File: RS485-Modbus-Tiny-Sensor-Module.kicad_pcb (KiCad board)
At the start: 2 copper layers, 10 parts, among them SW1 FSM4JSMA, U2 ATtiny3216-S

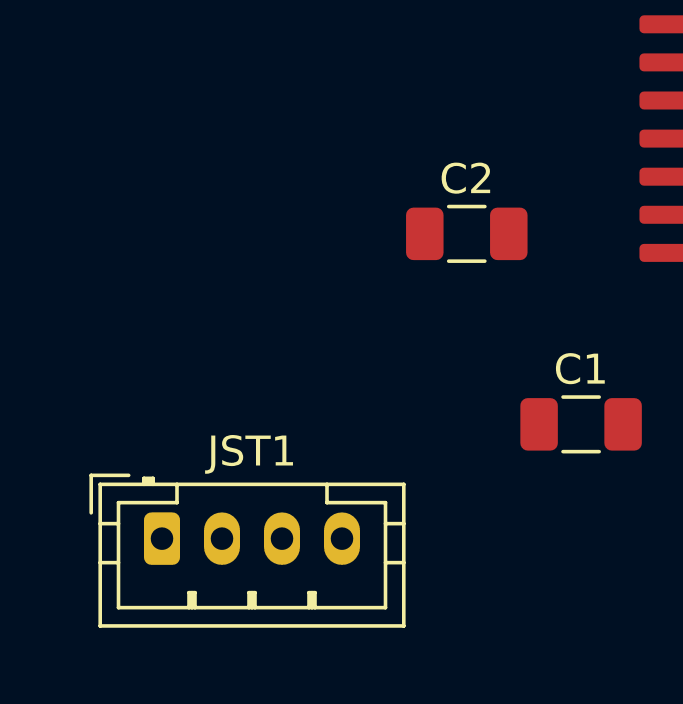
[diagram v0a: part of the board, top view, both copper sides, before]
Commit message: Add files via upload
Changed JST connection to smallest + fix connection to 3.3 V
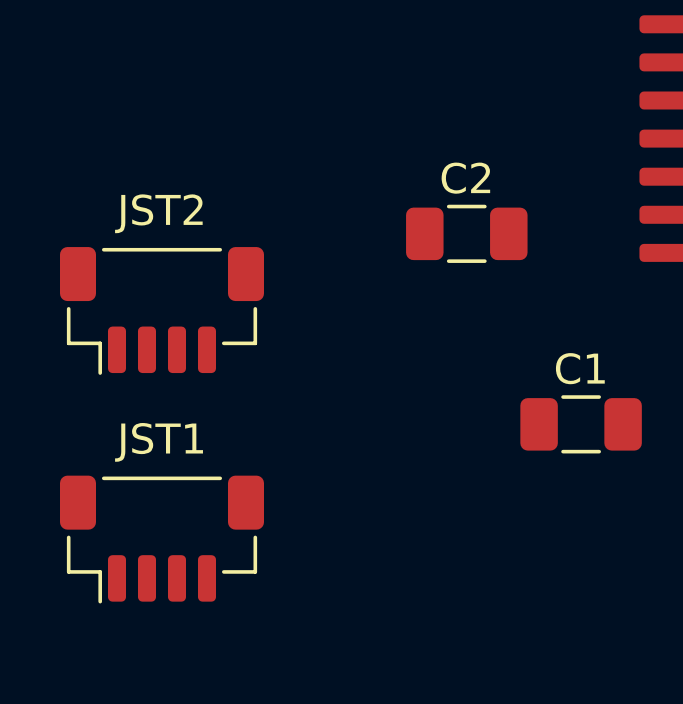
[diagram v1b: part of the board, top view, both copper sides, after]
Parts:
- added JST2: Conn_01x04, Connector_JST:JST_SH_BM04B-SRSS-TB_1x04-1MP_P1.00mm_Vertical, F.Cu at (99.1, 105.4)
- JST1: footprint Connector_JST:JST_PH_B4B-PH-K_1x04_P2.00mm_Vertical -> Connector_JST:JST_SH_BM04B-SRSS-TB_1x04-1MP_P1.00mm_Vertical
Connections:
- U2 pad 1: Net-(U2-Pad1) -> /3.3V

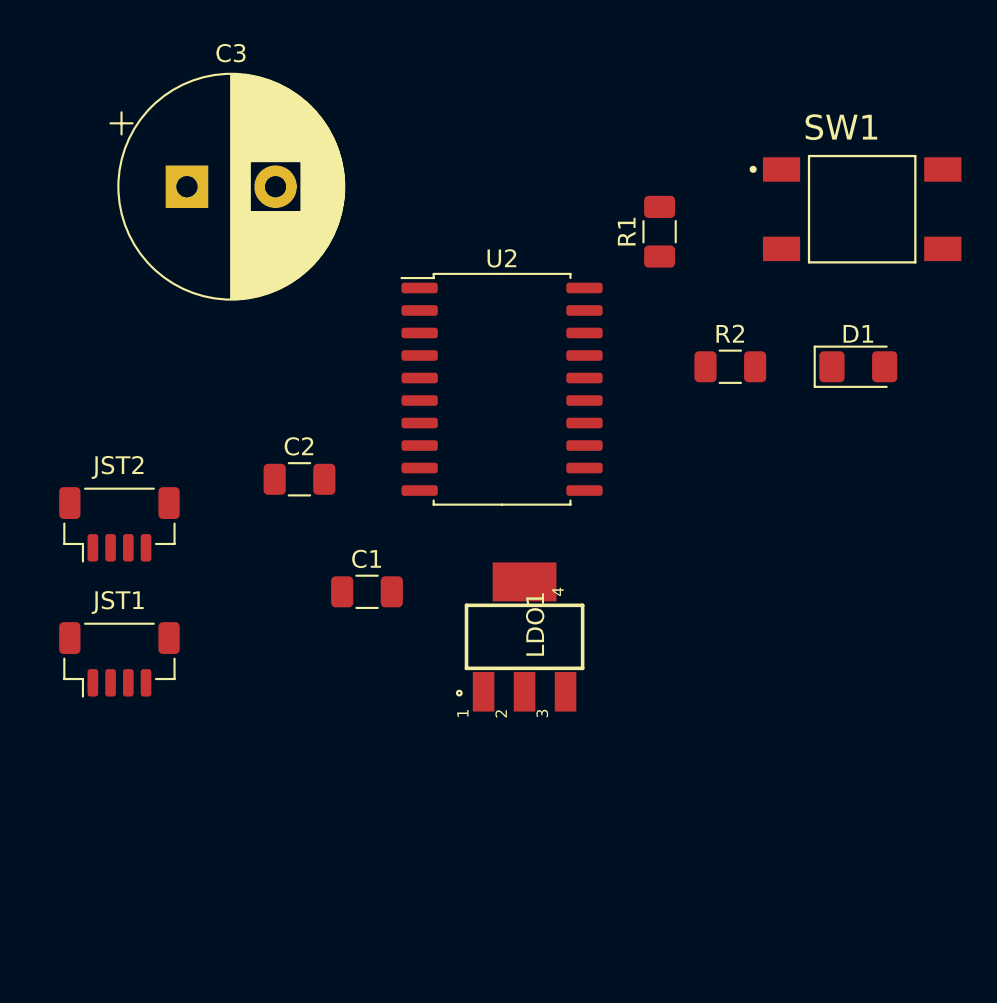
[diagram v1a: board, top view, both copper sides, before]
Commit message: Add files via upload
Added 24V LDO + cleaned layout + added autoreset
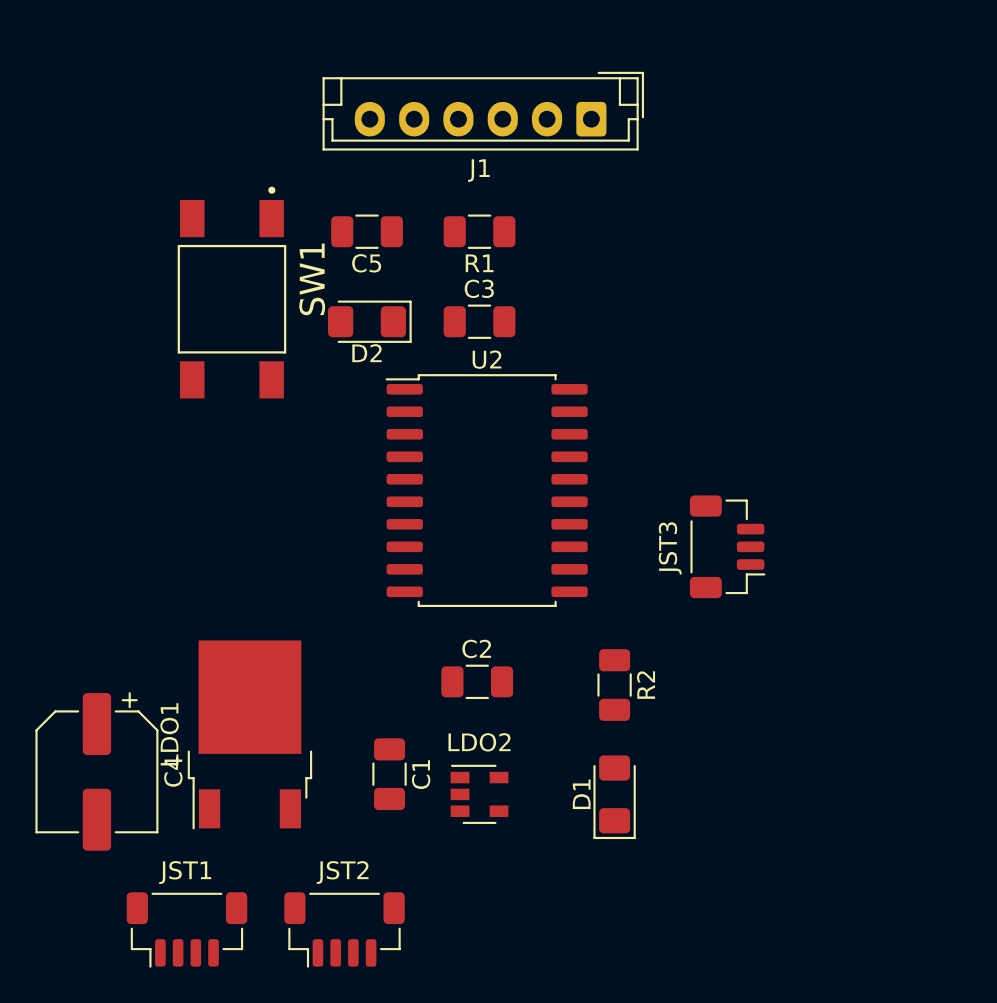
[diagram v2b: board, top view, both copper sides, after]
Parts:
- added C4: 100u, Capacitor_SMD:CP_Elec_6.3x7.7, F.Cu at (97.8, 119.4)
- added C5: 10u, Capacitor_SMD:C_1206_3216Metric, F.Cu at (113.0, 88.9)
- added D2: D, Diode_SMD:D_1206_3216Metric_Pad1.42x1.75mm_HandSolder, F.Cu at (113.0, 94.0)
- added J1: Conn_01x06, Connector_JST:JST_EH_B6B-EH-A_1x06_P2.50mm_Vertical, F.Cu at (125.7, 82.5)
- added JST3: Conn_01x03, Connector_JST:JST_SH_BM03B-SRSS-TB_1x03-1MP_P1.00mm_Vertical, F.Cu at (133.3, 106.7)
- added LDO2: MIC5504-3.3YM5, Package_TO_SOT_SMD:SOT-23-5, F.Cu at (119.4, 120.7)
- C1: value 10u -> 100u
- C3: value 2700u -> 100u; footprint Capacitor_THT:CP_Radial_D12.5mm_P5.00mm -> Capacitor_SMD:C_1206_3216Metric
- LDO1: value LM1117IMP-5.0-NOPB -> LD1086DT50TR; footprint LM1117IMP-5:SOT223 -> Package_TO_SOT_SMD:TO-252-2
- R2: value 200 -> 300
- moved SW1 35.9 mm to (105.4, 92.7), turned to 270 degrees
- moved D1 27.8 mm to (127.0, 120.7), turned to 90 degrees
- moved JST2 26.2 mm to (111.8, 128.3)
- moved R2 19.1 mm to (127.0, 114.5), turned to 270 degrees
- moved C3 18.2 mm to (119.4, 94.0)
- moved LDO1 16.4 mm to (106.4, 117.3)
- moved JST1 15.7 mm to (102.9, 128.3)
- moved C2 15.2 mm to (119.2, 114.3)
- moved C1 10.4 mm to (114.3, 119.5), turned to 270 degrees
- moved R1 10.2 mm to (119.4, 88.9), turned to 180 degrees
- moved U2 5.78 mm to (119.8, 103.5)
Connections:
- JST1 pad 2: /5V -> /24V
- JST2 pad 2: /5V -> /24V
- LDO1 pad 2: /3.3V -> /5V
- LDO1 pad 3: /5V -> /24V
- R1 pad 1: /3.3V -> /5V
- U2 pad 1: /3.3V -> /5V
- U2 pad 12: Net-(U2-Pad12) -> Net-(R2-Pad1)
- U2 pad 5: Net-(U2-Pad5) -> /PA7
- U2 pad 8: Net-(U2-Pad8) -> /RX
- U2 pad 9: Net-(U2-Pad9) -> /TX

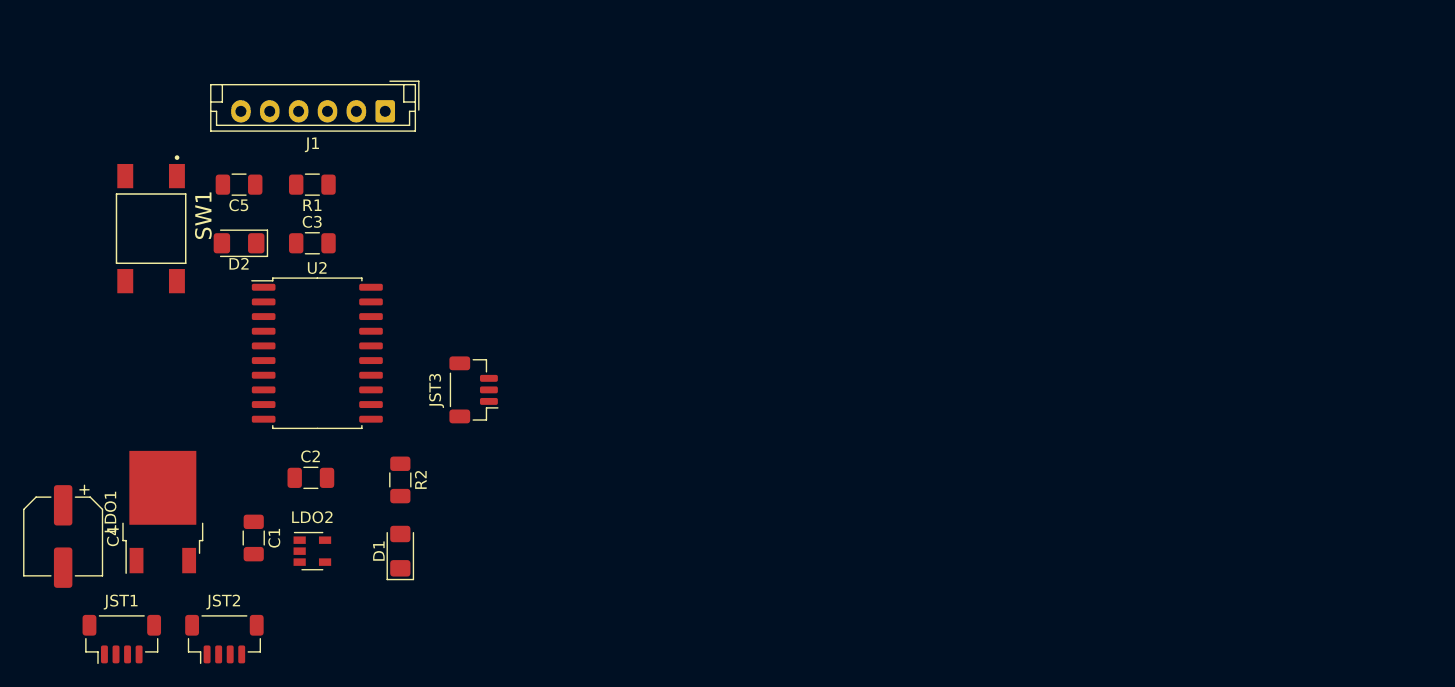
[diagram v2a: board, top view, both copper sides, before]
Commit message: Add files via upload
Finished layout prototype + added extra JST
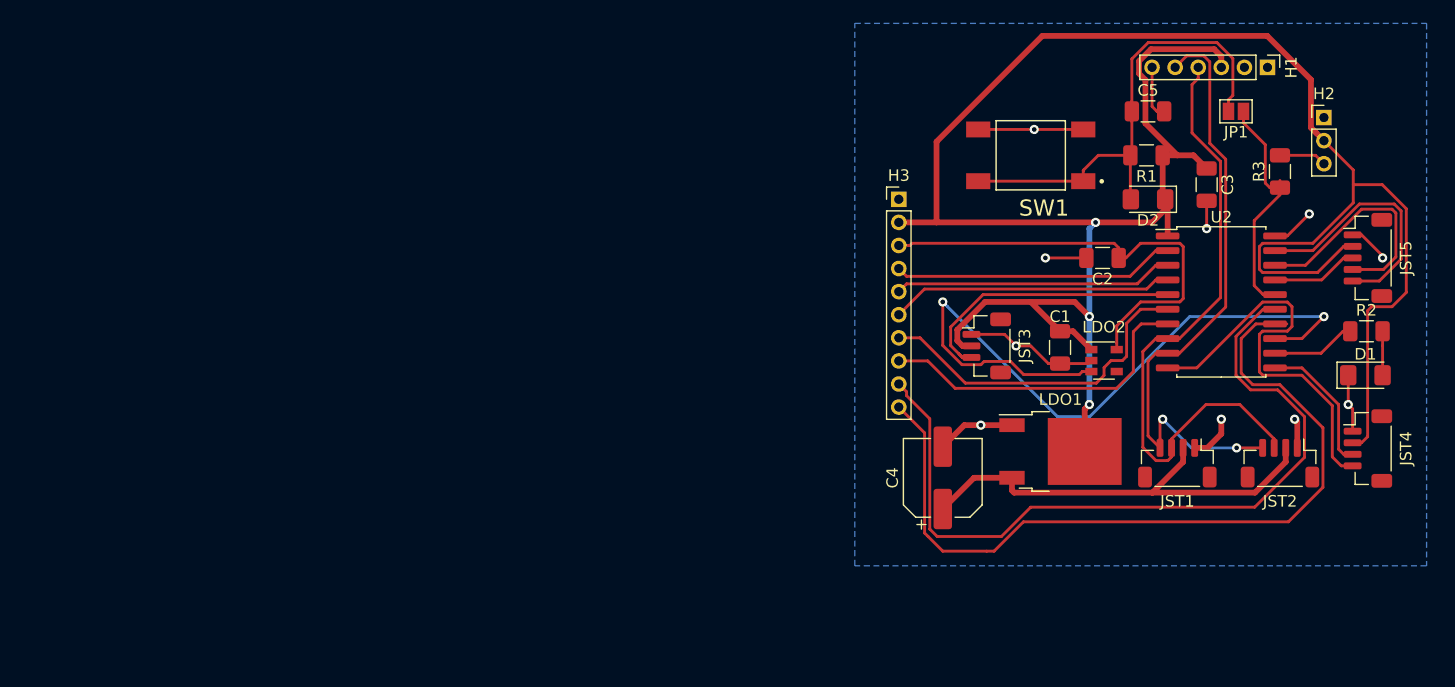
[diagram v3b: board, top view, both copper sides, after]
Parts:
- added H2: Conn_01x03, Connector_PinHeader_2.00mm:PinHeader_1x03_P2.00mm_Vertical, F.Cu at (207.0, 83.1)
- added H3: Conn_01x10, Connector_PinHeader_2.00mm:PinHeader_1x10_P2.00mm_Vertical, F.Cu at (170.2, 90.2)
- added JP1: Jumper, Jumper:SolderJumper-2_P1.3mm_Open_Pad1.0x1.5mm, F.Cu at (199.4, 82.5)
- added JST4: Conn_01x04, Connector_JST:JST_SH_BM04B-SRSS-TB_1x04-1MP_P1.00mm_Vertical, F.Cu at (210.8, 111.8)
- added JST5: Conn_01x05, Connector_JST:JST_SH_BM05B-SRSS-TB_1x05-1MP_P1.00mm_Vertical, F.Cu at (210.8, 95.2)
- added R3: 4.7k, Resistor_SMD:R_1206_3216Metric, F.Cu at (203.2, 87.8)
- C5: value 10u -> 1u
- H1: renamed from J1; footprint Connector_JST:JST_EH_B6B-EH-A_1x06_P2.50mm_Vertical -> Connector_PinHeader_2.00mm:PinHeader_1x06_P2.00mm_Vertical
- moved JST1 92.7 mm to (194.3, 113.0), turned to 180 degrees
- moved JST2 92.7 mm to (203.2, 113.0), turned to 180 degrees
- moved D1 85.0 mm to (210.6, 105.4), turned to 0 degrees
- moved R2 84.7 mm to (210.7, 101.6), turned to 0 degrees
- moved C5 79.0 mm to (191.8, 82.5), turned to 0 degrees
- moved D2 78.8 mm to (191.8, 90.2)
- moved U2 78.4 mm to (198.1, 99.1)
- moved LDO1 77.9 mm to (184.2, 112.0), turned to 0 degrees
- moved C3 77.6 mm to (196.8, 88.9), turned to 270 degrees
- moved H1 76.5 mm to (202.1, 78.7), turned to 270 degrees
- moved SW1 76.5 mm to (181.6, 86.4), turned to 180 degrees
- moved C4 76.4 mm to (174.0, 114.3), turned to 90 degrees
- moved R1 72.3 mm to (191.6, 86.4)
- moved C1 71.8 mm to (184.2, 103.0)
- moved C2 71.2 mm to (187.8, 95.2), turned to 180 degrees
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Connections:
- JST1 pad 3: Net-(JST1-Pad3) -> /RX
- JST1 pad 4: Net-(JST1-Pad4) -> /TX
- JST2 pad 3: Net-(JST2-Pad3) -> /RX
- JST2 pad 4: Net-(JST2-Pad4) -> /TX
- U2 pad 10: Net-(U2-Pad10) -> /SDA
- U2 pad 11: Net-(U2-Pad11) -> /SCL
- U2 pad 14: Net-(U2-Pad14) -> /PC2
- U2 pad 15: Net-(U2-Pad15) -> /PC3
- U2 pad 16: Net-(C5-Pad1) -> /RST
- U2 pad 17: Net-(U2-Pad17) -> /MOSI
- U2 pad 18: Net-(U2-Pad18) -> /MISO
- U2 pad 19: Net-(U2-Pad19) -> /SCK
- U2 pad 2: Net-(U2-Pad2) -> /PA4
- U2 pad 3: Net-(U2-Pad3) -> /PA5
- U2 pad 4: Net-(U2-Pad4) -> /PA6
- U2 pad 6: Net-(U2-Pad6) -> /PB5
- U2 pad 7: Net-(U2-Pad7) -> /PB4
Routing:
- net /5V: track 0.00 -> 203.6 mm, vias 0 -> 3
- net /PC2: track 0.00 -> 71.0 mm
- net /PC3: track 0.00 -> 67.9 mm
- net Net-(LDO2-Pad3): track 0.00 -> 63.8 mm, vias 0 -> 2
- net /TX: track 0.00 -> 55.1 mm, vias 0 -> 2
- net /RX: track 0.00 -> 54.9 mm
- net /GND: track 0.00 -> 52.7 mm, vias 0 -> 10
- net Net-(C5-Pad1): track 0.00 -> 42.7 mm
- net /3.3V: track 0.00 -> 39.7 mm
- net /24V: track 0.00 -> 39.3 mm
- net /SDA: track 0.00 -> 35.4 mm
- net /PB5: track 0.00 -> 29.6 mm
- net /PB4: track 0.00 -> 28.6 mm
- net /PA6: track 0.00 -> 24.5 mm
- net /PA4: track 0.00 -> 24.5 mm
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- added copper zone on B.Cu, net /GND
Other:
- net class Second added: clearance 0.2, trace_width 0.5, via_dia 0.8, via_drill 0.4

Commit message: Add files via upload
Added BOM + .zip file that contains files for production of PCB
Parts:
- JP1: footprint Jumper:SolderJumper-2_P1.3mm_Open_Pad1.0x1.5mm -> Resistor_SMD:R_0805_2012Metric
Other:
- board outline added: 49.5 x 47 mm
- board text added: "3.3V"
- board text added: "5V"
- board text added: "DTR"
- board text added: "GND"
- board text added: "MISO"
- board text added: "MOSI"
- board text added: "PA4"
- board text added: "PA5"
- board text added: "PA6"
- board text added: "PA7"
- board text added: "PB4"
- board text added: "PB5"
- board text added: "PC2"
- board text added: "PC3"
- board text added: "RX"
- board text added: "SCK"
- board text added: "SCL"
- board text added: "SDA"
- board text added: "TX"
- board text added: "UPDI/RST"

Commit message: Add files via upload
PCB V1.0
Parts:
- removed C5: 1u, Capacitor_SMD:C_1206_3216Metric
- removed D2: D, Diode_SMD:D_1206_3216Metric_Pad1.42x1.75mm_HandSolder
- removed H2: Conn_01x03, Connector_PinHeader_2.00mm:PinHeader_1x03_P2.00mm_Vertical
- removed H3: Conn_01x10, Connector_PinHeader_2.00mm:PinHeader_1x10_P2.00mm_Vertical
- removed JP1: Jumper, Resistor_SMD:R_0805_2012Metric
- removed the R1 at (191.6, 86.4)
- removed SW1: FSM4JSMA, FSM4JSMA:TE_FSM4JSMA
- added UPDI1: Conn_01x03, Connector_JST:JST_SH_SM03B-SRSS-TB_1x03-1MP_P1.00mm_Horizontal, F.Cu at (186.7, 94.0)
- 1-Wire1: renamed from JST3; footprint Connector_JST:JST_SH_BM03B-SRSS-TB_1x03-1MP_P1.00mm_Vertical -> Connector_JST:JST_SH_SM03B-SRSS-TB_1x03-1MP_P1.00mm_Horizontal
- C1, C2, LDO1, LDO2: moved to B.Cu
- H1: value Conn_01x06 -> Conn_01x10; footprint Connector_PinHeader_2.00mm:PinHeader_1x06_P2.00mm_Vertical -> Connector_PinHeader_2.54mm:PinHeader_1x10_P2.54mm_Vertical
- I²C1: renamed from JST4; footprint Connector_JST:JST_SH_BM04B-SRSS-TB_1x04-1MP_P1.00mm_Vertical -> Connector_JST:JST_SH_SM04B-SRSS-TB_1x04-1MP_P1.00mm_Horizontal
- RS485: renamed from JST1; footprint Connector_JST:JST_SH_BM04B-SRSS-TB_1x04-1MP_P1.00mm_Vertical -> Connector_JST:JST_SH_SM04B-SRSS-TB_1x04-1MP_P1.00mm_Horizontal
- RS485_2: renamed from JST2; footprint Connector_JST:JST_SH_BM04B-SRSS-TB_1x04-1MP_P1.00mm_Vertical -> Connector_JST:JST_SH_SM04B-SRSS-TB_1x04-1MP_P1.00mm_Horizontal; moved to B.Cu
- SPI1: renamed from JST5; value Conn_01x05 -> Conn_01x06; footprint Connector_JST:JST_SH_BM05B-SRSS-TB_1x05-1MP_P1.00mm_Vertical -> Connector_JST:JST_SH_SM06B-SRSS-TB_1x06-1MP_P1.00mm_Horizontal
- moved LDO1 19.0 mm to (198.1, 99.1), turned to 90 degrees
- moved C1 18.0 mm to (198.0, 91.4), turned to 180 degrees
- moved H1 17.0 mm to (186.7, 85.9), turned to 90 degrees
- moved C4 16.9 mm to (190.5, 110.5)
- moved I²C1 10.5 mm to (208.3, 101.6), turned to 90 degrees
- moved 1-Wire1 8.98 mm to (186.7, 101.6)
- moved R2 7.99 mm to (195.6, 90.2), turned to 180 degrees
- moved D1 7.41 mm to (206.8, 111.8)
- moved R1 7.41 mm to (206.9, 108.0)
- moved LDO2 6.35 mm to (191.8, 99.1), turned to 180 degrees
- moved RS485 5.68 mm to (199.4, 110.5), turned to 0 degrees
- moved C3 5.24 mm to (201.9, 90.2), turned to 0 degrees
- moved RS485_2 4.58 mm to (199.4, 110.5)
- moved SPI1 3.59 mm to (208.3, 92.7), turned to 90 degrees
- moved C2 1.89 mm to (189.2, 94.0), turned to 90 degrees
- renumbered R2 to R1, R3 to R2
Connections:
- H1 pad 2: Net-(H1-Pad2) -> /5V
- H1 pad 3: /5V -> /3.3V
- H1 pad 4: /RX -> /PA6
- H1 pad 5: /TX -> /PA5
- H1 pad 6: /DTR -> /PA4
- R2 pad 2: /UPDI -> Net-(R2-Pad2)
- SPI1 pad 3: /MOSI -> /3.3V
- SPI1 pad 4: /MISO -> /MOSI
- SPI1 pad 5: /SCK -> /MISO
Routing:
- net /5V: track 203.6 -> 88.9 mm, vias 3 -> 4
- net Net-(LDO2-Pad3): track 63.8 -> 10.8 mm, vias 2 -> 1
- net /PC2: track 71.0 -> 21.8 mm
- net /PC3: track 67.9 -> 22.6 mm
- net Net-(C5-Pad1): track 42.7 -> 0.00 mm
- net /TX: track 55.1 -> 19.3 mm, vias 2 -> 1
- net /RX: track 54.9 -> 24.7 mm, vias 0 -> 1
- net /SDA: track 35.4 -> 15.2 mm
- net /24V: track 39.3 -> 21.6 mm, vias 0 -> 1
- net /PA7: track 24.3 -> 7.23 mm
- net /SCK: track 22.0 -> 6.91 mm
- net /MISO: track 20.6 -> 7.01 mm
- net Net-(R2-Pad2): track 0.00 -> 10.9 mm
- net /PB5: track 29.6 -> 19.5 mm
- net /3.3V: track 39.7 -> 47.2 mm, vias 0 -> 2
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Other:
- board size 49.5 x 47 mm -> 30.5 x 31.8 mm
- board text added: "24V"
- board text added: "GND 5V 3.3V PA6 PA5 PA4 PB5 PB4 PC3 PC2"
- board text added: "V1.0"
- board text removed: "DTR"
- board text removed: "MISO"
- board text removed: "MOSI"
- board text removed: "PA4"
- board text removed: "PA5"
- board text removed: "PA6"
- board text removed: "PB4"
- board text removed: "PB5"
- board text removed: "PC2"
- board text removed: "PC3"
- board text removed: "SCK"
- board text removed: "SCL"
- board text removed: "SDA"
- board text removed: "UPDI/RST"
